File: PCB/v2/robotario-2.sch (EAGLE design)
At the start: 27 parts, among them T1 2N3904, T2 2N3904, U1 ATTINY85-20PU

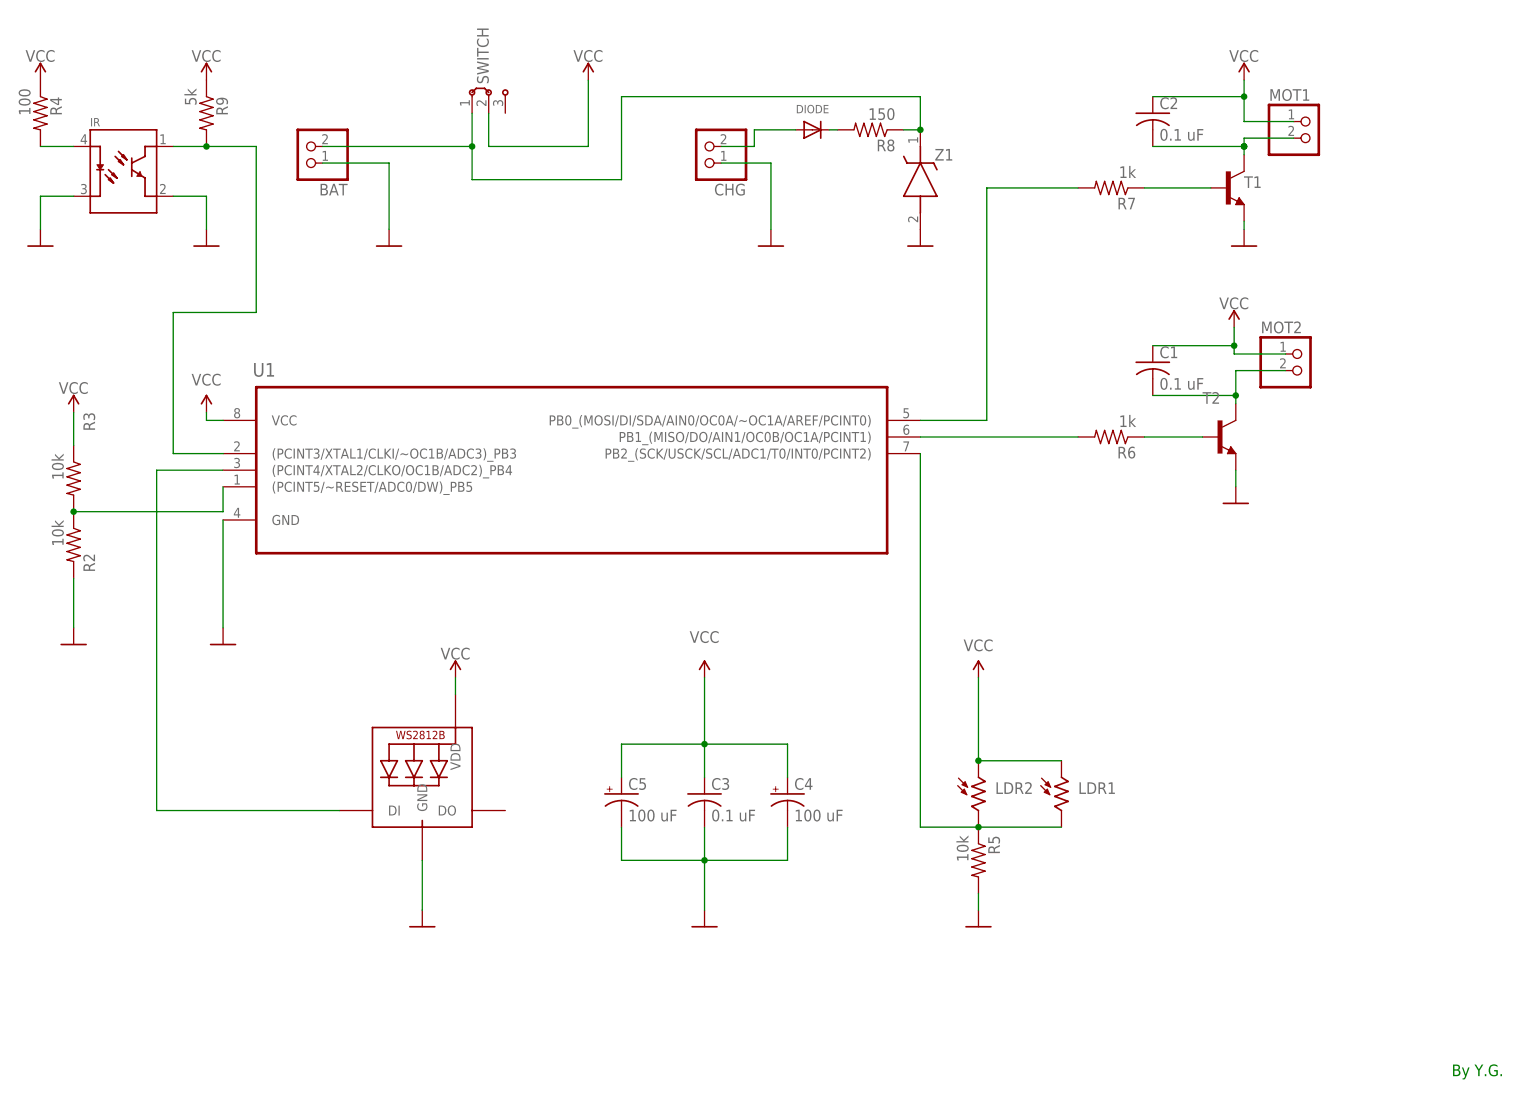
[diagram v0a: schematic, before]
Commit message: added software tests
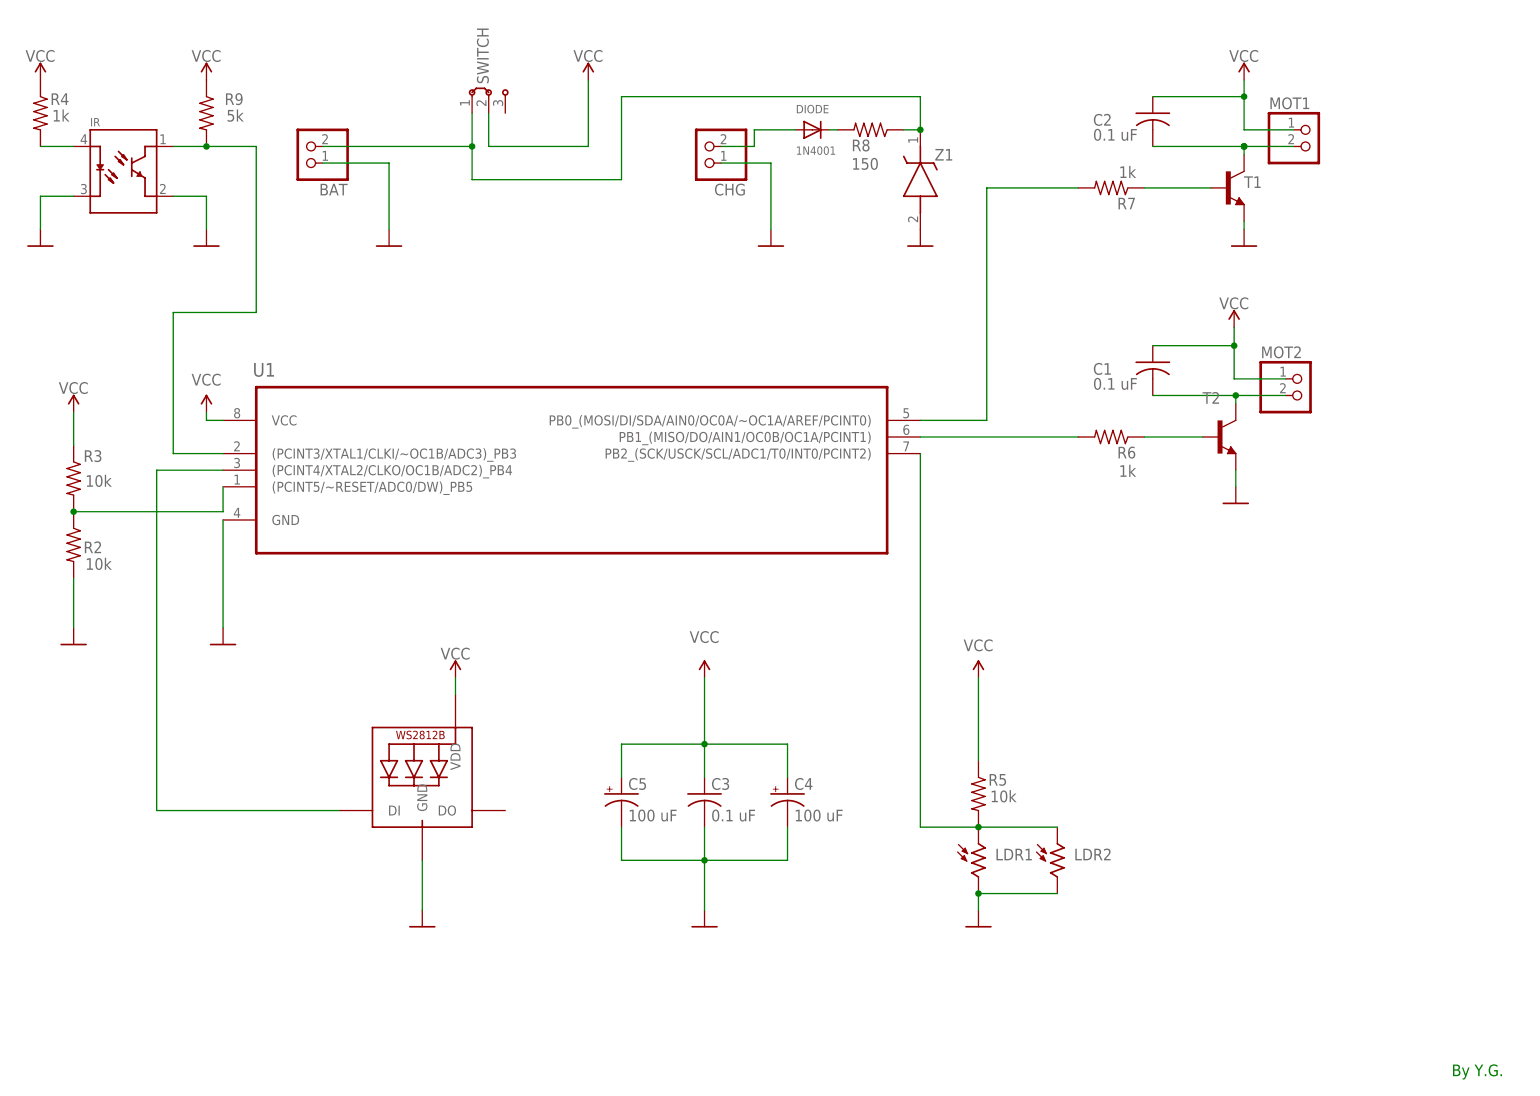
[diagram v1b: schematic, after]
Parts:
- DIODE: value (none) -> 1N4001
- R4: value 100 -> 1k
- renumbered LED2 to LED1
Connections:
- net GND: now also LDR1.2, LDR2.2; no longer R5.2
- net N$6: now also LDR1.1, LDR2.1, R5.2; no longer LDR1.2, LDR2.2, R5.1
- net VCC: now also R5.1; no longer LDR1.1, LDR2.1
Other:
- moved on the sheet: LDR1, LDR2, MOT1, MOT2, R5
